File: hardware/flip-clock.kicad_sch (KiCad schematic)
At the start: 19 parts, among them J1 Screw_Terminal_01x02, J2 Conn_01x04, Q1 TCRT5000, U1 WeMos_D1_mini

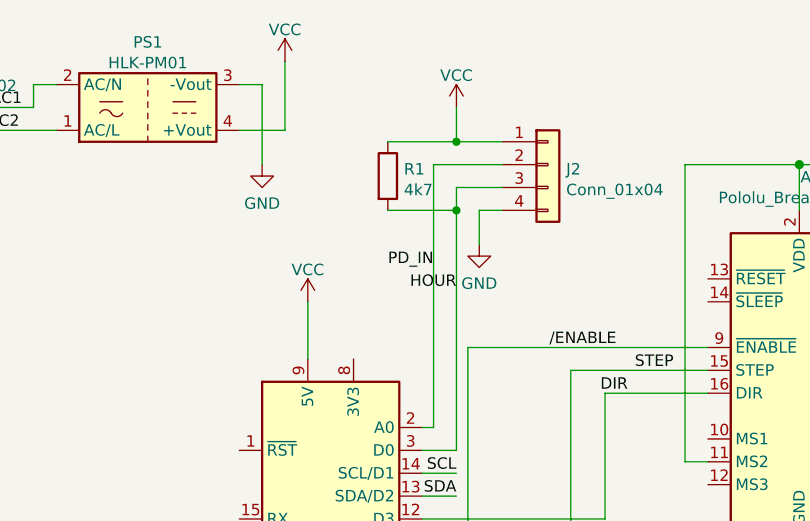
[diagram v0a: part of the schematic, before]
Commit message: Use 3v3 as stable power supply for IR-Sensor
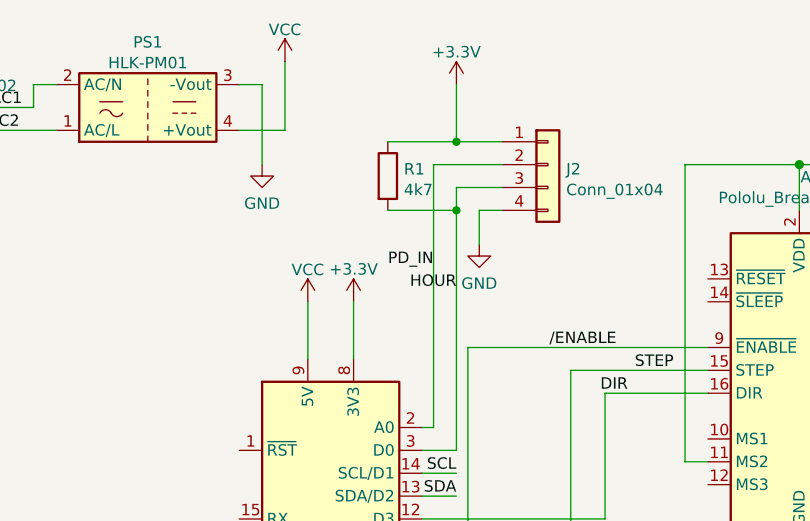
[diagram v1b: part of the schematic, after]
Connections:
- net VCC: no longer J2.1 (Pin_1), R1.1
- net +3V3: now reaches U1.8 (3V3)
- net +3V3: now also J2.1 (Pin_1), R1.1
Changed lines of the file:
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@@
   (junction (at 43.18 119.38) (diameter 0.9144) (color 0 0 0 0)
   )
+  (wire (pts (xy 106.68 50.8) (xy 106.68 57.15))
+    (stroke (width 0) (type default) (color 0 0 0 0))
+  )
   (wire (pts (xy 101.6 50.8) (xy 101.6 57.15))
     (stroke (width 0) (type solid) (color 0 0 0 0))
@@
     (stroke (width 0) (type solid) (color 0 0 0 0))
   )
-  (wire (pts (xy 118.11 29.21) (xy 118.11 33.02))
+  (wire (pts (xy 118.11 26.67) (xy 118.11 33.02))
     (stroke (width 0) (type solid) (color 0 0 0 0))
   )
@@
     (pin "1")
   )
+  (symbol (lib_id "power:+3.3V") (at 118.11 26.67 0) (unit 1)
+    (in_bom yes) (on_board yes) (fields_autoplaced)
+    (property "Reference" "#PWR?" (id 0) (at 118.11 30.48 0)
+      (effects (font (size 1.27 1.27)) hide)
+    )
+    (property "Value" "+3.3V" (id 1) (at 118.11 23.0655 0))
+    (property "Footprint" "" (id 2) (at 118.11 26.67 0)
+      (effects (font (size 1.27 1.27)) hide)
+    )
+    (property "Datasheet" "" (id 3) (at 118.11 26.67 0)
+      (effects (font (size 1.27 1.27)) hide)
+    )
+    (pin "1")
+  )
+  (symbol (lib_id "power:+3.3V") (at 106.68 50.8 0) (unit 1)
+    (in_bom yes) (on_board yes) (fields_autoplaced)
+    (property "Reference" "#PWR?" (id 0) (at 106.68 54.61 0)
+      (effects (font (size 1.27 1.27)) hide)
+    )
+    (property "Value" "+3.3V" (id 1) (at 106.68 47.1955 0))
+    (property "Footprint" "" (id 2) (at 106.68 50.8 0)
+      (effects (font (size 1.27 1.27)) hide)
+    )
+    (property "Datasheet" "" (id 3) (at 106.68 50.8 0)
+      (effects (font (size 1.27 1.27)) hide)
+    )
+    (pin "1")
+  )
   (symbol (lib_id "power:GND") (at 21.59 40.64 0) (unit 1)
     (in_bom yes) (on_board yes) (fields_autoplaced)
@@
     )
     (property "Datasheet" "~" (id 3) (at 180.34 54.61 0)
-      (effects (font (size 1.27 1.27)) hide)
-    )
-    (pin "1")
-  )
-  (symbol (lib_id "power:VCC") (at 118.11 29.21 0) (unit 1)
-    (in_bom yes) (on_board yes) (fields_autoplaced)
-    (property "Reference" "#PWR04" (id 0) (at 118.11 33.02 0)
-      (effects (font (size 1.27 1.27)) hide)
-    )
-    (property "Value" "VCC" (id 1) (at 118.11 25.6626 0))
-    (property "Footprint" "" (id 2) (at 118.11 29.21 0)
-      (effects (font (size 1.27 1.27)) hide)
-    )
-    (property "Datasheet" "" (id 3) (at 118.11 29.21 0)
       (effects (font (size 1.27 1.27)) hide)
     )
@@
       (reference "#PWR03") (unit 1) (value "GND") (footprint "")
     )
-    (path "/f885ed0e-b62e-4614-9701-70ede6c1ad6a"
-      (reference "#PWR04") (unit 1) (value "VCC") (footprint "")
-    )
     (path "/43b22163-7452-4c9c-a7b2-e40e2d3d7e2a"
       (reference "#PWR05") (unit 1) (value "GND") (footprint "")
@@
       (reference "#PWR0104") (unit 1) (value "GND") (footprint "")
     )
+    (path "/e0b09194-c95a-4fcd-af7c-326f7d8dc882"
+      (reference "#PWR?") (unit 1) (value "+3.3V") (footprint "")
+    )
+    (path "/e7e6cb6d-7647-4949-b7bd-8bc1e899dd19"
+      (reference "#PWR?") (unit 1) (value "+3.3V") (footprint "")
+    )
     (path "/afa3bd6a-7e18-4e83-97e0-c36ee46dea5c"

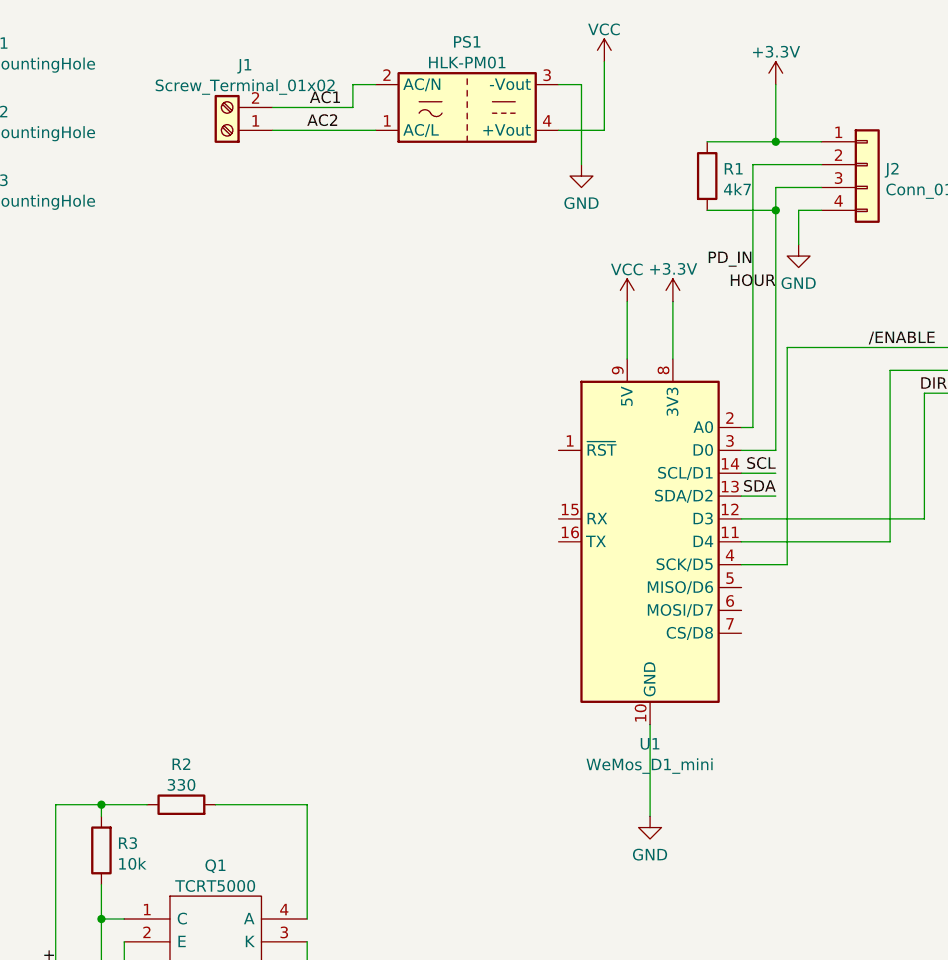
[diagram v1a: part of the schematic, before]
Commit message: Adds detection of rising and falling edge
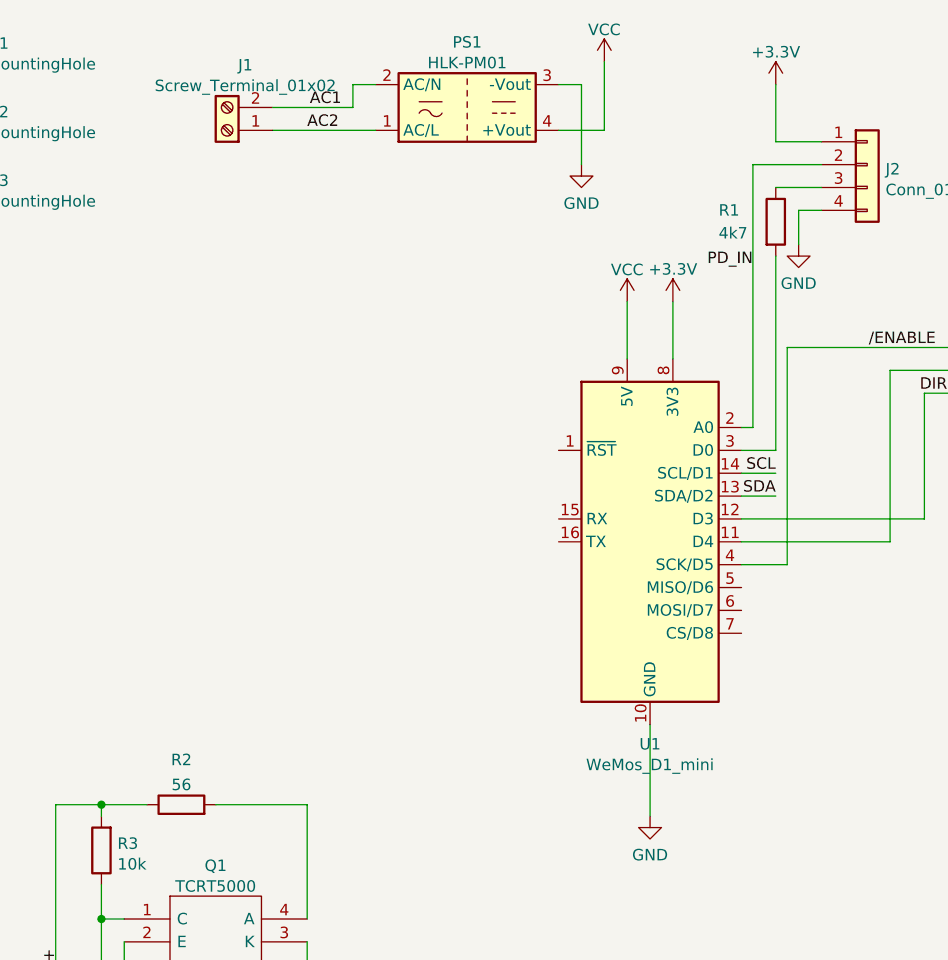
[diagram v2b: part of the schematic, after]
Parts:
- R2: value 330 -> 56
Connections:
- net +3V3: no longer R1.1
- net HOUR: no longer names the net of R1.2, U1.3 (D0)
- net HOUR: no longer J2.3 (Pin_3)
- new net: J2.3 (Pin_3), R1.1
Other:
- moved on the sheet: R1
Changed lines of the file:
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@@
   (junction (at 43.18 106.68) (diameter 0.9144) (color 0 0 0 0)
   )
-  (junction (at 118.11 33.02) (diameter 0.9144) (color 0 0 0 0)
-  )
   (junction (at 161.29 35.56) (diameter 1.016) (color 0 0 0 0)
-  )
-  (junction (at 118.11 40.64) (diameter 0.9144) (color 0 0 0 0)
   )
   (junction (at 43.18 119.38) (diameter 0.9144) (color 0 0 0 0)
@@
     (stroke (width 0) (type solid) (color 0 0 0 0))
   )
-  (wire (pts (xy 118.11 40.64) (xy 118.11 38.1))
-    (stroke (width 0) (type solid) (color 0 0 0 0))
-  )
-  (wire (pts (xy 118.11 67.31) (xy 118.11 40.64))
-    (stroke (width 0) (type solid) (color 0 0 0 0))
-  )
   (wire (pts (xy 62.23 31.75) (xy 73.66 31.75))
     (stroke (width 0) (type solid) (color 0 0 0 0))
@@
     (stroke (width 0) (type solid) (color 0 0 0 0))
   )
-  (wire (pts (xy 110.49 33.02) (xy 118.11 33.02))
-    (stroke (width 0) (type solid) (color 0 0 0 0))
-  )
   (wire (pts (xy 134.62 60.96) (xy 146.05 60.96))
     (stroke (width 0) (type solid) (color 0 0 0 0))
@@
     (stroke (width 0) (type solid) (color 0 0 0 0))
   )
+  (wire (pts (xy 118.11 45.72) (xy 118.11 67.31))
+    (stroke (width 0) (type default) (color 0 0 0 0))
+  )
   (wire (pts (xy 156.21 35.56) (xy 156.21 40.64))
     (stroke (width 0) (type solid) (color 0 0 0 0))
@@
     (stroke (width 0) (type solid) (color 0 0 0 0))
   )
-  (wire (pts (xy 110.49 40.64) (xy 118.11 40.64))
-    (stroke (width 0) (type solid) (color 0 0 0 0))
-  )
   (wire (pts (xy 114.3 74.93) (xy 134.62 74.93))
     (stroke (width 0) (type solid) (color 0 0 0 0))
@@
   )
   (label "SDA" (at 118.11 72.39 180)
-    (effects (font (size 1.27 1.27)) (justify right bottom))
-  )
-  (label "HOUR" (at 118.11 49.53 180)
     (effects (font (size 1.27 1.27)) (justify right bottom))
   )
@@
   (symbol (lib_id "Device:R") (at 52.07 106.68 90) (unit 1)
     (in_bom yes) (on_board yes) (fields_autoplaced)
-    (property "Reference" "R2" (id 0) (at 52.07 102.2308 90))
-    (property "Value" "330" (id 1) (at 52.07 104.5295 90))
+    (property "Reference" "R2" (id 0) (at 52.07 101.6975 90))
+    (property "Value" "56" (id 1) (at 52.07 104.4726 90))
     (property "Footprint" "Resistor_SMD:R_0805_2012Metric" (id 2) (at 52.07 108.458 90)
       (effects (font (size 1.27 1.27)) hide)
@@
     (pin "2")
   )
-  (symbol (lib_id "Device:R") (at 110.49 36.83 0) (unit 1)
-    (in_bom yes) (on_board yes) (fields_autoplaced)
-    (property "Reference" "R1" (id 0) (at 112.2681 36.0691 0)
-      (effects (font (size 1.27 1.27)) (justify left))
-    )
-    (property "Value" "4k7" (id 1) (at 112.2681 38.3678 0)
-      (effects (font (size 1.27 1.27)) (justify left))
-    )
-    (property "Footprint" "Resistor_SMD:R_0805_2012Metric" (id 2) (at 108.712 36.83 90)
-      (effects (font (size 1.27 1.27)) hide)
-    )
-    (property "Datasheet" "~" (id 3) (at 110.49 36.83 0)
+  (symbol (lib_id "Device:R") (at 118.11 41.91 0) (unit 1)
+    (in_bom yes) (on_board yes)
+    (property "Reference" "R1" (id 0) (at 111.76 40.64 0)
+      (effects (font (size 1.27 1.27)) (justify left))
+    )
+    (property "Value" "4k7" (id 1) (at 111.76 43.18 0)
+      (effects (font (size 1.27 1.27)) (justify left))
+    )
+    (property "Footprint" "Resistor_SMD:R_0805_2012Metric" (id 2) (at 116.332 41.91 90)
+      (effects (font (size 1.27 1.27)) hide)
+    )
+    (property "Datasheet" "~" (id 3) (at 118.11 41.91 0)
       (effects (font (size 1.27 1.27)) hide)
     )
@@
     )
     (path "/5652473f-51c5-4709-afb9-0e50a9e46c96"
-      (reference "R2") (unit 1) (value "330") (footprint "Resistor_SMD:R_0805_2012Metric")
+      (reference "R2") (unit 1) (value "56") (footprint "Resistor_SMD:R_0805_2012Metric")
     )
     (path "/8712bf73-147b-43c1-b686-4964febb13cd"
